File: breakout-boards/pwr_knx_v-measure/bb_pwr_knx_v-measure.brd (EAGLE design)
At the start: 28.5 x 25 mm, 47 parts, among them IC100 BD9G101, T1 BC856, T2 BCP52, T3 BC847

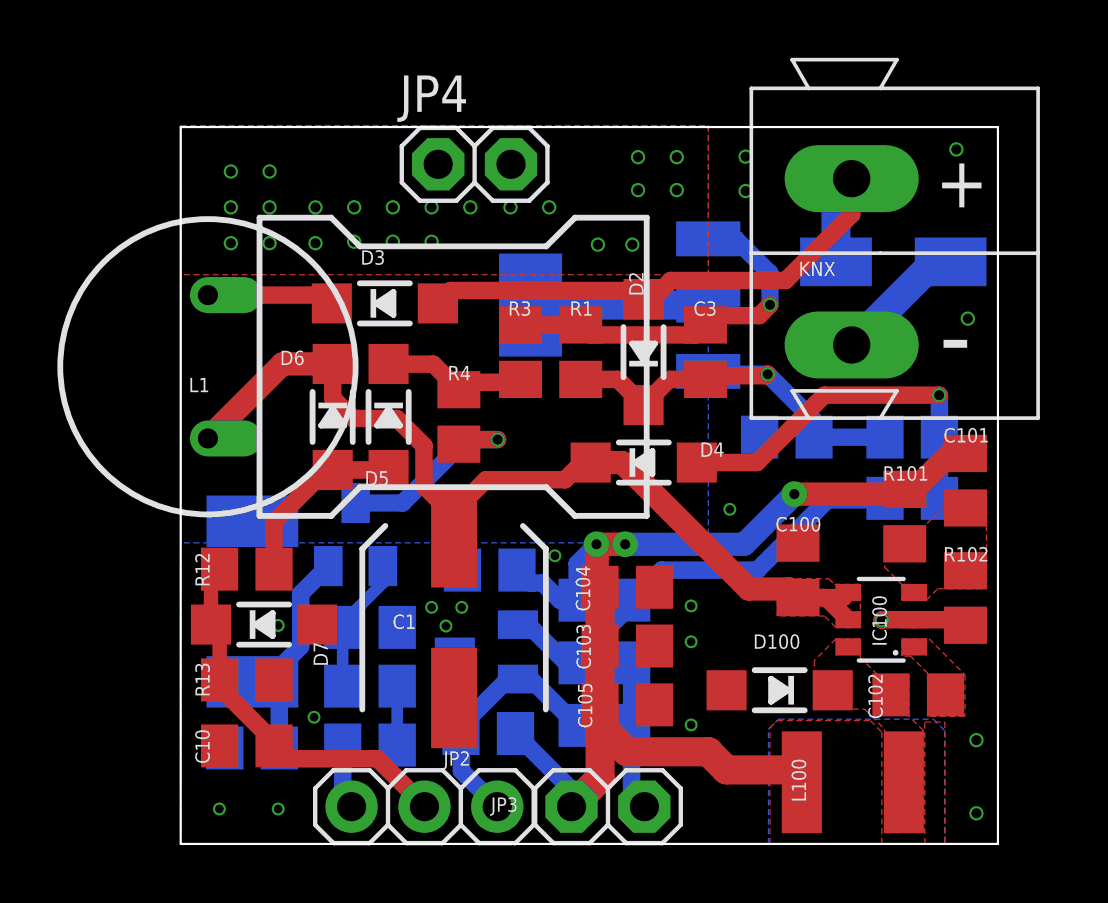
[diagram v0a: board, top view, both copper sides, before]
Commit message: [BB_Pwr+KNX] - rearranged parts colliding with IO module
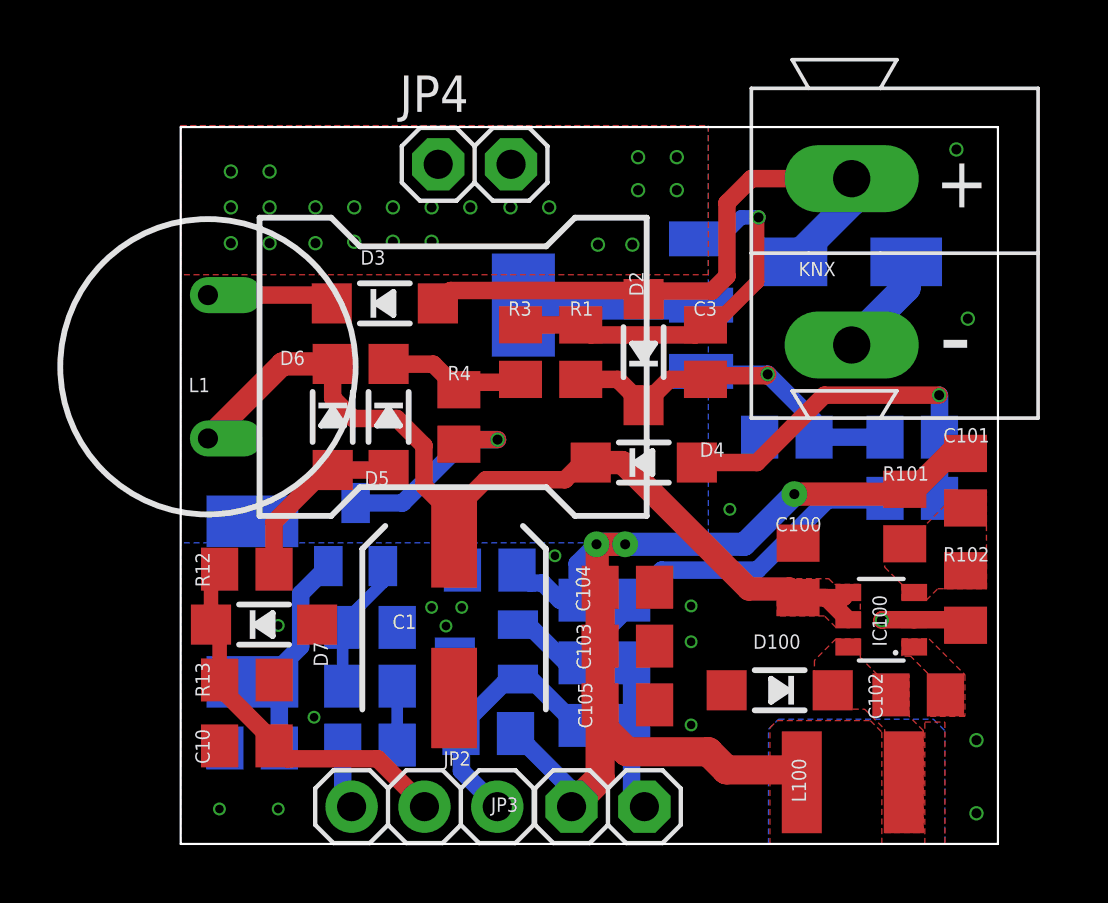
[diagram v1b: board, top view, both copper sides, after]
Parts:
- moved D1 1.55 mm to (24.8, 20.3)
- moved T2 0.25 mm to (16.5, 18.8)
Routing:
- net EIB+: track 20.7 -> 21.7 mm
- net GND: track 12.9 -> 11.9 mm, vias 19 -> 17
- net N$15: track 13.0 -> 13.7 mm
